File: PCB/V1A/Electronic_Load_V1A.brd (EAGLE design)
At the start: 230 x 150 mm, 139 parts, among them IC201 OPA77P, IC202 OPA77P, IC203 OPA77P, IC204 OPA77P, IC205 OPA77P, IC301 MAX743CPE, IC302 7805T, IC303 7805T, J101 +, J102 -, J103 +, J104 -, Q101 SIRC10DP, Q102 SIRC10DP, Q103 SIRC10DP, Q104 IXTK102N65X2PADUP-, Q105 SIRC10DP, Q106 SIRC10DP, Q107 SIRC10DP, Q108 IXTK102N65X2PADUP, U201 LTC1865-MSOP, U202 LTC1865-MSOP, U203 LTC1865-MSOP, U401 AD420, U402 AD420, U403 LT1014

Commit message: Board layout work
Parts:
- IC304: value (none) -> 7905
- R101, R102, R103, R104, R105, R109, R110, R111, R112: device rcl:M5923 -> rcl:R1206
- R107, R114: device rcl:R0805 -> rcl:R1206
- R403, R404, R405, R406, R407, R408, R409, R410: device rcl:M5923 -> rcl:R0805
- moved R211 359.8 mm to (-222.0, -74.0), turned to 270 degrees
- moved C205 352.2 mm to (-191.0, -55.0)
- moved C206 352.0 mm to (-191.0, -58.0)
- moved C210 340.3 mm to (-170.0, -60.0), turned to 270 degrees
- moved R201 340.1 mm to (-222.0, -50.0), turned to 270 degrees
- moved R217 336.5 mm to (-222.0, -84.0), turned to 90 degrees
- moved C209 334.4 mm to (-174.0, -60.0), turned to 270 degrees
- moved R202 333.4 mm to (-222.0, -46.0), turned to 270 degrees
- moved R216 332.2 mm to (-222.0, -78.0), turned to 90 degrees
- moved R212 331.8 mm to (-222.0, -70.0), turned to 270 degrees
- moved C204 331.6 mm to (-191.0, -28.0)
- moved R221 330.3 mm to (-212.0, -84.0), turned to 90 degrees
- moved R220 329.0 mm to (-217.0, -81.0)
- moved U202 328.3 mm to (-180.0, -60.0), turned to 270 degrees
- moved R203 326.8 mm to (-222.0, -42.0), turned to 270 degrees
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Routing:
- net CSENSE_L2: track 0.00 -> 3.79 mm
- net CSENSE_L1: track 0.00 -> 3.79 mm
- net CSENSE_H2: track 0.00 -> 3.79 mm
- net CSENSE_H1: track 0.00 -> 3.79 mm
- net N$61: track 0.00 -> 1.99 mm, vias 0 -> 1
- net N$58: track 0.00 -> 1.99 mm, vias 0 -> 1
- net N$60: track 0.00 -> 1.87 mm, vias 0 -> 1
- net N$57: track 0.00 -> 1.87 mm, vias 0 -> 1
- net N$56: track 0.00 -> 1.87 mm, vias 0 -> 1
- net N$55: track 0.00 -> 1.87 mm, vias 0 -> 1
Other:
- board size 230 x 150 mm -> 220 x 151 mm

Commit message: Board layout work
PCB is 100x100mm 2 layer 2oz. MOSFETs mounted between a plate and heatsinks, control board mounted under the plate. DUT+ connected directly from binding post to drains, gates and sources connected to PCB with wires.
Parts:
- added PAD1, PAD2, PAD3, PAD4: PAD-5X2, pads:PAD-5X2
- added PAD5, PAD6, PAD7: PAD-10X4, pads:PAD-10X4
- moved R226 293.1 mm to (91.0, 16.0)
- moved R216 276.6 mm to (39.0, 13.5), turned to 270 degrees
- moved R217 276.3 mm to (35.0, 17.5), turned to 270 degrees
- moved R203 275.6 mm to (47.0, 18.0)
- moved R202 275.5 mm to (47.0, 13.5)
- moved R201 275.4 mm to (47.0, 9.00)
- moved R208 275.3 mm to (47.0, 4.50)
- moved R209 275.2 mm to (47.0, 0.00)
- moved R211 273.9 mm to (39.0, 9.00), turned to 90 degrees
- moved R210 271.9 mm to (43.0, -1.00), turned to 0 degrees
- moved R212 271.4 mm to (39.0, 4.50), turned to 90 degrees
- moved R213 269.2 mm to (39.0, 0.00), turned to 90 degrees
- moved R220 268.4 mm to (34.0, 14.0), turned to 180 degrees
- moved R221 264.7 mm to (32.5, 17.5), turned to 270 degrees
- moved R224 253.5 mm to (29.5, 22.0), turned to 270 degrees
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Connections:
- net CSENSE_L1: now also PAD7.1
- net CSENSE_L2: now also PAD6.1
- net GND: now also PAD5.1
- net N$52: now also PAD3.1
- net N$54: now also PAD4.1
- net VSENSE+: now also PAD1.1
- net VSENSE-: now also PAD2.1
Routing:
- net GND: track 0.00 -> 26.4 mm, vias 0 -> 1
- net VSENSE-: track 0.00 -> 14.2 mm
- net VSENSE: track 0.00 -> 13.6 mm
- net CSENSE_H1: track 3.79 -> 15.6 mm
- net N$92: track 0.00 -> 11.6 mm
- net VSENSE+: track 0.00 -> 11.3 mm
- net +5V: track 0.00 -> 10.2 mm, vias 0 -> 1
- net CSENSE_H2: track 3.79 -> 12.6 mm
- net N$91: track 0.00 -> 7.00 mm
- net N$62: track 0.00 -> 6.81 mm
- net CSENSE_L1: track 3.79 -> 7.31 mm
- net N$85: track 0.00 -> 3.07 mm
- net N$84: track 0.00 -> 3.07 mm
- net N$89: track 0.00 -> 2.60 mm
- net N$88: track 0.00 -> 2.60 mm
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- removed copper zone on layer 1, net DUT_+1
- removed copper zone on layer 16, net DUT_+1
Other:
- board size 220 x 151 mm -> 100 x 100 mm
- board text added: "Current sense/bypass drivers"
- board text added: "DUT-"
- board text added: "G_Q1"
- board text added: "G_Q2"
- board text added: "Gate drivers/DACs"
- board text added: "Remote sense"
- board text added: "S_Q1"
- board text added: "S_Q2"
- board text added: "VSENSE+"
- board text added: "VSENSE-"

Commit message: Added temp sensors
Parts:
- added C1, C3, C411, C412: 0.1µ, rcl:C0805
- added C2: 1µ, rcl:C0805
- added PAD103, PAD104: PAD-5X2, pads:PAD-5X2
- added Q401, Q403: BC817-25SMD, transistor-npn:SOT23-BEC
- added Q402: BC807-25SMD, transistor-pnp:SOT23-BEC
- added R1, R2, R411, R412, R413: 5k, rcl:R0805
- added R3, R4, R5: 10k, rcl:R0805
- added U1: LTC1865-MSOP, adc_dac:MSOP-10
- C301, C310, C311, L301, L302: value 100u -> 100µ
- C302, C401, C402, C409, C410: value 100n -> 0.1µ
- C303, C315: value 1u -> 1µ
- C305: value 10u -> 10µ
- C307, C312: value 0.33u -> 0.33µ
- C308, C314: value 0.1u -> 0.1µ
- C309: value 22u -> 22µ
- C313: value 2u2 -> 2µ2
- C403: value 10n -> 0.1µ
- C407: value 100n -> 10n
- C408: value 100n -> 500p
- R401: value 20k -> 1k; device rcl:RTRIM4G/J -> rcl:R1206
- R402: value 20k -> 10k; device rcl:RTRIM4G/J -> rcl:R1206
- R403: value 200k -> 1k; device rcl:R0805 -> rcl:R1206
- R404: value 200k -> 20k; device rcl:R0805 -> rcl:RTRIM4G/J
- R405: value 100R -> 20k; device rcl:R0805 -> rcl:RTRIM4G/J
- R406: value 100R -> 200k
- R407: value 5k -> 200k
- R408, R409: value 5k -> 100R
- moved R403 236.7 mm to (-173.0, -198.0)
- moved C403 232.4 mm to (-168.0, -198.0)
- moved R402 232.1 mm to (-183.0, -198.0)
- moved R401 226.3 mm to (-178.0, -198.0)
- moved C408 188.3 mm to (-170.0, -190.0)
- moved PAD2 81.6 mm to (-39.0, 8.00), turned to 0 degrees
- moved PAD1 78.4 mm to (-39.0, 16.0), turned to 0 degrees
- moved C404 30.0 mm to (-118.0, 29.0)
- moved C406 30.0 mm to (-118.0, 25.0)
- moved C410 29.4 mm to (-118.0, -9.00)
- moved C405 26.0 mm to (-118.0, -1.00)
- moved C407 26.0 mm to (-118.0, -5.00)
- moved C409 25.6 mm to (-118.0, 21.0)
- moved R404 15.7 mm to (-74.0, 3.00)
- moved R405 13.0 mm to (-67.0, 3.00)
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- renumbered PAD3 to PAD101, PAD4 to PAD105, PAD5 to PAD107, PAD6 to PAD106, PAD7 to PAD102
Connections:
- removed net +IN: U403.12, U403.14
- removed net -IN: U403.11, U403.15
- removed net OUT: U403.10, U403.16
- new net BYP_CTRL: C408.2, R403.1
- new net CLR_DAC1: U401.6
- new net CLR_DAC2: U402.6
- new net DAC1_OUT: U401.10, U402.9
- new net DAC2_OUT: U402.10
- new net DAC_FAULT: R5.1, U401.3, U402.3
- new net N$47: R2.2, R4.1, U403.15
- new net N$49: R1.2, R3.1, U403.11
- new net N$93: Q401.B, Q402.B, Q403.C, R401.1
- new net N$94: C403.1, Q401.C, R401.2, R402.2
- new net N$95: C403.2, Q402.C, Q403.E
- new net N$96: C408.1, Q403.B, R402.1, R403.2
- new net SS_ADC_T: U1.1
- new net SS_DAC: U401.7, U402.7
- new net TEMP1_AMP: R3.2, U1.2, U403.10
- new net TEMP1_IN: PAD1.1, U403.12
- new net TEMP2_AMP: R4.2, U1.3, U403.16
- new net TEMP2_IN: PAD2.1, U403.14
- net +12V: now also C407.2, C409.1, C410.1; no longer C403.2, C407.1, C408.1
- net +15V: now also C411.1; no longer C409.1
- net +5V: now also C1.1, C2.1, R5.2, U1.9
- net +5V/1: now also R404.3, R405.3; no longer R401.3, R402.3
- net -15V: now also C412.1; no longer C410.1
- net -5V: now also C3.2, R404.1, R405.1; no longer R401.1, R402.1
- net BYP_G: now also Q401.E, Q402.E
- net GND: now also C1.2, C2.2, C3.1, C411.2, C412.2, R1.1, R2.1, R408.1, R409.1, U1.4, U1.5; no longer C407.2, C408.2, R405.1, R406.1
- net LOAD_G1: now also R412.2; no longer R409.2
- net LOAD_G2: now also R413.2; no longer R410.2
- net MISO: now also U1.7
- net MOSI: now also U1.6, U401.9
- net N$24: now also C407.1; no longer C406.1
- net N$25: now also C404.1; no longer C403.1
- net N$26: now also C405.1; no longer C404.1
- net N$27: now also C406.1; no longer C405.1
- net N$28: now also R410.2, R412.1; no longer R407.2, R409.1
- net N$29: now also R411.2, R413.1; no longer R408.2, R410.1
- net N$32: now also R406.2, R408.2, R410.1; no longer R403.2, R405.2, R407.1
- net N$33: now also R404.2, R406.1; no longer R401.2, R403.1
- net N$34: now also R405.2, R407.1; no longer R402.2, R404.1
- net N$35: now also R407.2, R409.2, R411.1; no longer R404.2, R406.2, R408.1
- net SCK: now also U1.8, U401.8, U402.8
- net VREF: now also U1.10
- net VSENSE+: now also PAD103.1; no longer PAD1.1
- net VSENSE-: now also PAD104.1; no longer PAD2.1
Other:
- outline, holes or cut-outs redrawn
- board text added: "TEMP1"
- board text added: "TEMP2"

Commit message: Changed packages, board layout
Changed component packages and values to the ones that are available. Moved the heatsink mount back to the PCB,
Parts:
- added PAD3: PAD-10X4, pads:PAD-10X4
- C1, C201, C202, C203, C204, C205, C206, C208, C210, C211, C212, C213, C214, C216, C3, C302, C307, C308, C312, C314, C401, C402, C403, C408, C409, C411, C412: device rcl:C0805 -> rcl:C1206
- C2: device rcl:C0805 -> rcl:SMC_A
- C207, C209, C215: device rcl:SMC_C -> rcl:SMC_A
- C301, C310, C311: value 100µ -> 220µ; device rcl:085CS_1AR -> rcl:E3,5-10
- C303, C313, C315: device rcl:085CS_1AR -> rcl:SMC_A
- C305: device rcl:085CS_1AR -> rcl:SMC_C
- C309: device rcl:085CS_1AR -> rcl:SMC_D
- Q104: value IXTK102N65X2PADUP- -> IXTK102N65X2PADUP; device transistors:TO-264P-H-PADUP- -> transistors:TO-264P-H-PADUP
- R1, R2, R204, R205, R206, R207, R217, R220, R221, R224, R225, R227, R228, R229, R230, R3, R4, R410, R411, R412, R413, R5: device rcl:R0805 -> rcl:R0603
- R201, R202, R203, R208, R209, R210, R211, R212, R213, R214, R215, R216, R218, R219, R231, R232, R233, R234, R406, R407, R408, R409: device rcl:R0805 -> rcl:R1206
- R401, R402, R403: device rcl:R1206 -> rcl:R0603
- moved R210 309.4 mm to (-266.0, -17.0)
- moved R209 309.4 mm to (-262.0, -15.0)
- moved R213 309.4 mm to (-270.0, -15.0)
- moved R208 309.3 mm to (-262.0, -9.50)
- moved R212 309.3 mm to (-270.0, -9.50)
- moved R201 309.3 mm to (-262.0, -4.00)
- moved R211 309.3 mm to (-270.0, -4.00)
- moved R202 309.2 mm to (-262.0, 1.50)
- moved R216 309.2 mm to (-270.0, 1.50)
- moved R203 309.2 mm to (-262.0, 7.00)
- moved C201 309.2 mm to (-326.0, -80.0)
- moved C202 309.2 mm to (-326.0, -107.0)
- moved C203 309.2 mm to (-326.0, -77.0)
- moved C204 309.2 mm to (-326.0, -110.0)
- moved C205 309.2 mm to (-285.5, 4.00)
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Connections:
- net +5V: now also C2.+; no longer C2.1
- net DUT_+1: now also PAD3.1
- net GND: now also C2.-; no longer C2.2
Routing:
- net GND: track 26.4 -> 9.29 mm
- net CSENSE_H1: track 15.6 -> 0.00 mm
- net VSENSE-: track 14.2 -> 0.00 mm
- net CSENSE_H2: track 12.6 -> 0.00 mm
- net VSENSE+: track 11.3 -> 1.08 mm
- net CSENSE_L1: track 7.31 -> 0.00 mm
- net CSENSE_L2: track 4.29 -> 0.00 mm
- net N$62: track 6.81 -> 7.63 mm
- added copper zone on layer 16, net DUT_+1
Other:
- board size 100 x 100 mm -> 180 x 225 mm
- board text added: "DUT+"

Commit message: Updated part list
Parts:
- removed PAD3: PAD-10X4, pads:PAD-10X4
- removed R1: 5k, rcl:R0603
- removed R5: 10k, rcl:R0603
- added C415, C416: 0.1µ, rcl:C1206
- added IC305, IC306: LM50, linear:SOT23
- added IC401: OPA77P, burr-brown:DIL08
- added PAD108: PAD-10X4, pads:PAD-10X4
- added R415, R416: 5k, rcl:R0603
- added R419, R420, R421, R422: 20k, rcl:R0603
- added R423: 20k, rcl:RTRIM4G/J
- R404: value 20k -> 10k; device rcl:RTRIM4G/J -> rcl:R0603
- R406: value 200k -> 20k; device rcl:R1206 -> rcl:RTRIM4G/J
- R408: value 100R -> 200k
- R410: value 5k -> 100R; device rcl:R0603 -> rcl:R1206
- moved R404 317.2 mm to (-184.0, -254.0)
- moved R413 279.4 mm to (-184.0, -205.0)
- moved R407 93.9 mm to (-463.5, 41.0)
- moved R409 93.9 mm to (-463.5, 38.0)
- moved R405 92.4 mm to (-451.0, 47.0)
- moved R411 90.4 mm to (-458.5, 38.0)
- moved U403 66.2 mm to (-449.5, 34.5)
- moved C411 65.5 mm to (-459.5, 35.1), turned to 180 degrees
- moved C412 52.1 mm to (-439.5, 35.1)
- moved U402 39.6 mm to (-424.0, 25.0), turned to 90 degrees
- moved C407 36.5 mm to (-433.0, 21.0), turned to 180 degrees
- moved C405 35.5 mm to (-433.0, 24.0), turned to 180 degrees
- moved C410 34.6 mm to (-424.0, 15.5)
- moved C402 29.9 mm to (-415.5, 20.6), turned to 90 degrees
- moved U401 28.9 mm to (-424.0, 44.0), turned to 90 degrees
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- renumbered C1 to C413, C2 to C414, C3 to C316, PAD1 to PAD401, PAD2 to PAD402, R2 to R414, R3 to R417, R4 to R418, U1 to U404
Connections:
- removed net N$32 (its old number): R406.2, R408.2, R410.1
- removed net N$33 (its old number): R404.2, R406.1
- new net N$34: R406.2, R408.1
- new net N$35: R408.2, R410.2, R412.1
- new net N$48: IC401.3, R420.1, R421.2
- new net N$50: R419.2, R421.1, R422.2
- new net N$51: IC401.8, R423.3
- new net N$53: IC401.1, R423.1
- new net N$90: U404.10
- new net TEMP1: IC305.2
- new net TEMP2: IC306.2
- new net VREF3.0: IC401.2, IC401.6
- net +15V: now also C415.1, IC401.7, R423.2
- net +5V: now also IC305.1, IC306.1, R404.2; no longer R5.2
- net +5V/1: now also R406.3; no longer R404.3
- net -15V: now also C416.1, IC401.4
- net -5V: now also R406.1; no longer R404.1
- net DAC_FAULT: now also R404.1; no longer R5.1
- net DUT_+1: now also PAD107.1; no longer PAD3.1
- net GND: now also C415.2, C416.2, IC305.3, IC306.3, PAD108.1, R410.1, R413.1, R419.1, R422.1; no longer PAD107.1, R1.1, R408.1
- net LOAD_G1: now also R415.2; no longer R412.2
- net LOAD_G2: now also R416.2; no longer R413.2
- net N$28: now also R411.2, R415.1; no longer R410.2, R412.1
- net N$29: now also R412.2, R416.1; no longer R411.2, R413.1
- net N$49: now also R413.2; no longer R1.2
- net VREF: now also R420.2; no longer U404.10
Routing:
- net +12V: track 0.00 -> 32.8 mm
- net VGATE_1: track 0.00 -> 29.3 mm
- net VGATE_2: track 0.00 -> 28.3 mm
- net GND: track 9.29 -> 33.5 mm, vias 1 -> 9
- net +5V: track 9.88 -> 16.9 mm
- net N$32: track 0.00 -> 5.73 mm
- net -15V: track 2.32 -> 6.02 mm
- net +15V: track 2.34 -> 6.03 mm
- net N$26: track 0.00 -> 3.40 mm
- net N$25: track 0.00 -> 3.40 mm
- net N$28: track 0.00 -> 3.38 mm
- net N$27: track 0.00 -> 3.36 mm
- net N$24: track 0.00 -> 3.36 mm
- net VREF: track 0.00 -> 1.27 mm

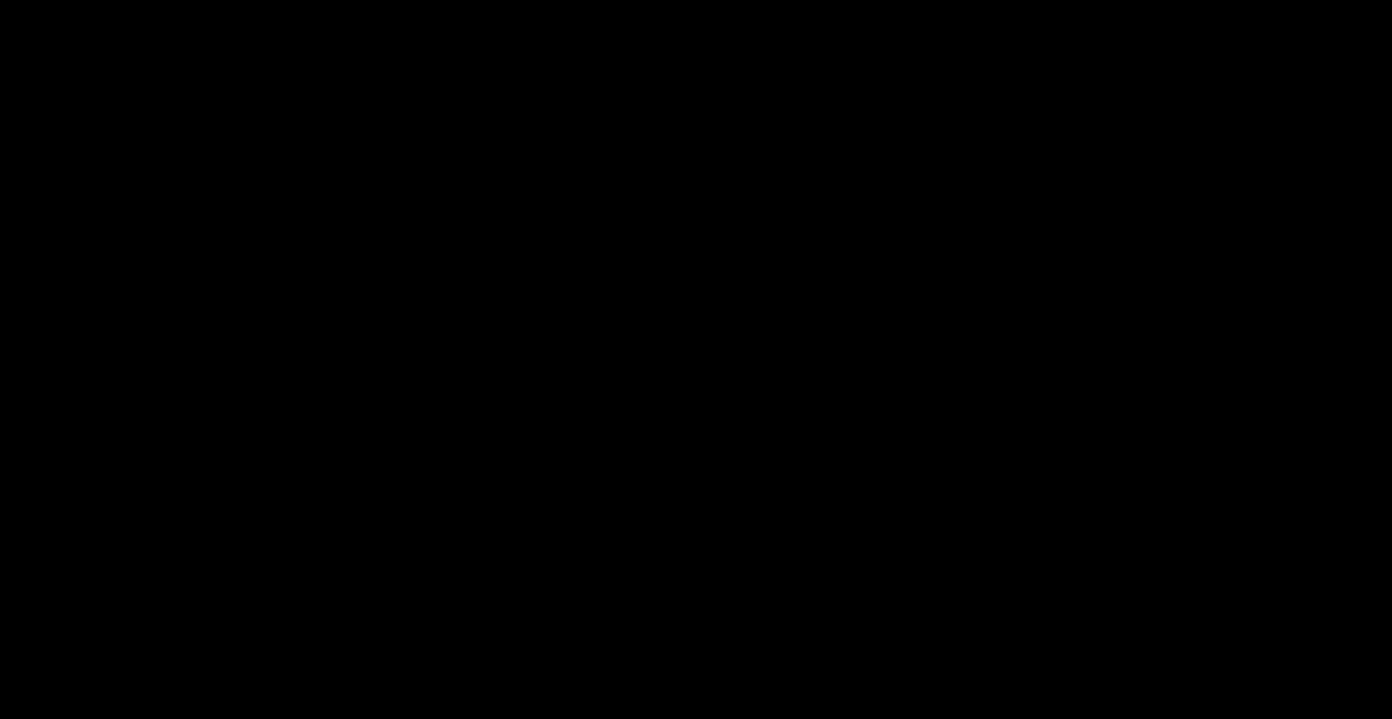
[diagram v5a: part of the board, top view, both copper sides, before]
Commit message: Changed OPA77 to AD620
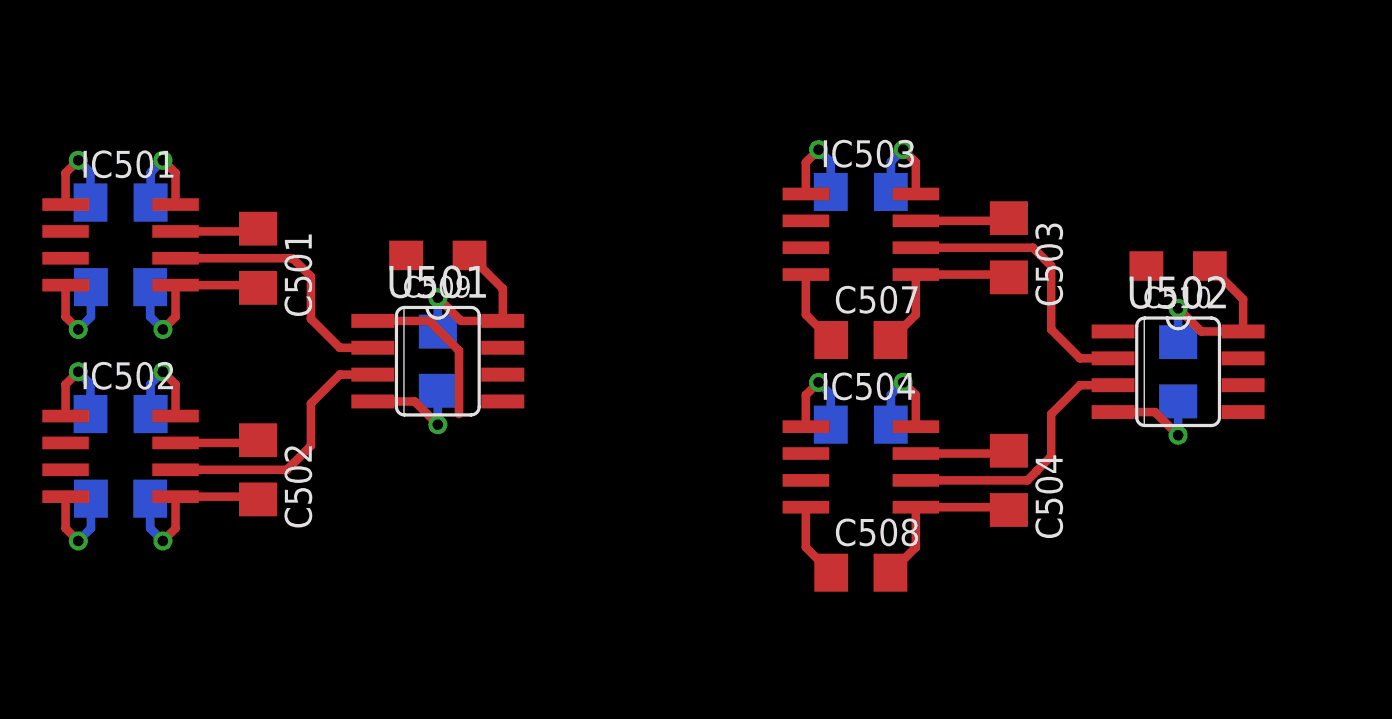
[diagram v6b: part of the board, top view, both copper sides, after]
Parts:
- added C501, C502, C503, C504, C505, C506, C507, C508, C511, C512: 0.1µ, rcl:C1206
- added C509, C510: 1µ, rcl:SMC_A
- added IC501, IC502, IC503, IC504: AD620R, analog-devices:SO8
- added R501, R502, R503, R504: 2k61, rcl:R1206
- added U501, U502: LTC1865L, adc_dac:SO08
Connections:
- new net +3V3: C509.+, C510.+, C511.1, C512.1, U501.8, U502.8
- new net CSENSE_H1_AMP1: IC503.6, U502.2
- new net CSENSE_H2_AMP1: IC504.6, U502.3
- new net MISO_ISO: U501.6, U502.6
- new net MOSI_ISO: U501.5, U502.5
- new net RG1_H1: IC501.1, R501.2
- new net RG1_H2: IC502.1, R502.2
- new net RG1_L1: IC503.1, R503.2
- new net RG1_L2: IC504.1, R504.2
- new net RG2_H1: IC501.8, R501.1
- new net RG2_H2: IC502.8, R502.1
- new net RG2_L1: IC503.8, R503.1
- new net RG2_L2: IC504.8, R504.1
- new net SCK_ISO: U501.7, U502.7
- new net SS_CH_ISO: U501.1
- new net SS_CL_ISO: U502.1
- net +15V: now also C501.1, C502.1, C503.1, C504.1, IC501.7, IC502.7, IC503.7, IC504.7
- net -15V: now also C505.1, C506.1, C507.1, C508.1, IC501.4, IC502.4, IC503.4, IC504.4
- net CSENSE_H1: now also IC501.3, IC503.2
- net CSENSE_H1_AMP: now also IC501.6, U501.2
- net CSENSE_H2: now also IC502.3, IC504.2
- net CSENSE_H2_AMP: now also IC502.6, U501.3
- net CSENSE_L1: now also IC503.3
- net CSENSE_L2: now also IC504.3
- net GND: now also C501.2, C502.2, C503.2, C504.2, C505.2, C506.2, C507.2, C508.2, C509.-, C510.-, C511.2, C512.2, IC501.2, IC501.5, IC502.2, IC502.5, IC503.5, IC504.5, U501.4, U502.4
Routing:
- net GND: track 33.5 -> 76.9 mm, vias 9 -> 13
- net +3V3: track 0.00 -> 17.7 mm, vias 0 -> 2
- net +15V: track 6.03 -> 22.8 mm
- net -15V: track 6.02 -> 22.4 mm, vias 0 -> 2
- net CSENSE_H1_AMP1: track 0.00 -> 13.3 mm
- net CSENSE_H2_AMP1: track 0.00 -> 12.4 mm
- net CSENSE_H2_AMP: track 0.00 -> 12.4 mm
- net CSENSE_H1_AMP: track 0.00 -> 12.3 mm
- net SS_CH_ISO: track 0.00 -> 7.66 mm
- net RG2_L2: track 0.00 -> 4.58 mm, vias 0 -> 1
- net RG2_L1: track 0.00 -> 4.58 mm, vias 0 -> 1
- net RG2_H2: track 0.00 -> 4.58 mm, vias 0 -> 1
- net RG2_H1: track 0.00 -> 4.58 mm, vias 0 -> 1
- net RG1_L2: track 0.00 -> 4.58 mm, vias 0 -> 1
- net RG1_L1: track 0.00 -> 4.58 mm, vias 0 -> 1
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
